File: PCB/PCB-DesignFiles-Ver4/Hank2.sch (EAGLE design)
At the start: 119 parts, among them T1 2n2222, T2 2n2222, T3 2n2222, T4 2n2222, T5 2n2222, T6 2n2222, T7 2n2222, T8 2n2222

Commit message: Mods added to pcb finished, now route the PCB
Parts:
- removed BREAKOUT: (no value), con-lstb:MA10-2
- removed C_OLED: 0.1uF, rcl:C-US025-024X044
- removed JTAG: (no value), con-lstb:MA03-2
- removed J_3V3V: Jumper, con-molex:22-23-2021
- removed LED1, LED2: (no value), led:LED3MM
- removed PR_5V1, PR_5V2, R_NI1, R_UTX1: 1k, rcl:R-US_0207/10
- removed R_NI2, R_UTX2: 2K, rcl:R-US_0207/10
- removed SSR1, SSR2, SSR3, SSR4, SSR5, SSR6, SSR7, SSR8: SSR, HankLibraries:SSR
- removed U$7: SD_CARD_READER, HankLibraries:SD_CARD_READER
- added ASC: LM358, SparkFun-IC-Amplifiers:LM358
- added C_RTC1: 0.1uF, rcl:C-US025-024X044
- added I2CR1, I2CR2: 4.7K, rcl:R-US_0207/10
- added I2C_BUS: (no value), con-lstb:MA04-1
- added LS11, LS12, LS21, LS22, LS31, LS32: 10K, rcl:R-US_0207/10
- added LSQ1, LSQ2, LSQ3: BSS138, adafruit:MOSFET-NREFLOW
- added SA1, SA2: 1k, rcl:R-US_0207/10
- added SAD1, SAD2: (no value), led:LED3MM
- added SC11: 51.5K, rcl:R-US_0207/10
- added SC12, SC22: 100k, rcl:R-US_0207/10
- added SC21: 51k1, rcl:R-US_0207/10
- added SV2, SV3: (no value), con-lstb:MA03-1
- added U$10, U$11, U$12, U$13, U$5, U$8, U$9: SSR, HankLibrariesV2:SSR
- added U$14: MA19-1, con-lstb:MA19-1
- added U$15: SD_CARD_READER, HankLibrariesV2:SD_CARD_READER
- RO12: value 150 -> 10k
- RO22, RO32, RO42, RO62, RO72, RO82: value 150 -> 10K
- U$1: value FLASH_MEMORY -> MA19-1; device HankLibraries:FLASH_MEMORY -> con-lstb:MA19-1
- U$4: value BLUETOOTH -> SSR; device HankLibraries:BLUETOOTH -> HankLibrariesV2:SSR
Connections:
- removed net FLASH_CLK: BREAKOUT.4, U$1.CLK
- removed net FLASH_CS: BREAKOUT.2, U$1.CS
- removed net FLASH_DI: BREAKOUT.6, U$1.DI
- removed net FLASH_DO: BREAKOUT.8, U$1.DO
- removed net N$1: BREAKOUT.1, J_5V-2.S
- removed net N$2: BREAKOUT.3, J_3V3V-2.S
- removed net N$39: IO_UC.(PCI2/SS/OC1B)PB2, R_NI1.2
- removed net NEW_IN: BREAKOUT.11, R_NI1.1, R_NI2.1
- removed net U_TX_3: BREAKOUT.15, R_UTX1.1, R_UTX2.2
- new net 3V3_OUT_ESP32: U$1.19, U$3.3V3
- new net 5V_BOARD: J_5V-2.S, U$1.1, U$3.5V
- new net EN_ESP32: U$1.18, U$3.EN
- new net L_AUTOMANUAL: LS31.1, LSQ3.S, U$1.9, U$3.IO27
- new net L_URX: LS11.1, LSQ1.S, U$14.9, U$3.IO17
- new net L_UTX: LS21.1, LSQ2.S, U$14.8, U$3.IO16
- new net N$38: SC21.2, SV2.3
- new net N$43: ASCG2.+IN, SC11.1, SC12.2
- new net N$44: ASCG1.+IN, SC21.1, SC22.2
- new net N$47: SC11.2, SV3.3
- new net PRESS_SEN1: ASCG2.-IN, ASCG2.OUT, U$1.17, U$3.SVP
- new net PRESS_SEN2: ASCG1.-IN, ASCG1.OUT, U$1.16, U$3.SVN
- new net SPARE_IO0: U$14.6, U$3.IO0
- new net SPARE_IO1: U$14.16, U$3.TXD0
- new net SPARE_IO10: U$1.3, U$3.SD3
- new net SPARE_IO11: U$1.2, U$3.CMD
- new net SPARE_IO12: U$1.7, U$3.IO12
- new net SPARE_IO13: U$1.5, U$3.IO13
- new net SPARE_IO14: U$1.8, U$3.IO14
- new net SPARE_IO15: U$14.4, U$3.IO15
- new net SPARE_IO2: U$14.5, U$3.IO2
- new net SPARE_IO3: U$14.15, U$3.RXD0
- new net SPARE_IO34: U$1.15, U$3.IO34
- new net SPARE_IO35: U$1.14, U$3.IO35
- new net SPARE_IO6: U$14.1, U$3.CLK
- new net SPARE_IO7: U$14.2, U$3.SD0
- new net SPARE_IO8: U$14.3, U$3.SD1
- new net SPARE_IO9: U$1.4, U$3.SD2
- new net U_SPARE: IO_UC.(PCI2/SS/OC1B)PB2
- net +3V3: now also C_RTC1.1, I2CR1.2, I2CR2.2, I2C_BUS.3, LS11.2, LS21.2, LS31.2, LSQ1.G, LSQ2.G, LSQ3.G, U$2.+3.3V; no longer C_OLED.1, C_USD.1, J_3V3V-1.S, U$1.+3.3V, U$1.HOLD, U$1.WP, U$4.+3.3V, U$7.+3.3V
- net +5V: now also ASCG3.P$V+, C_USD.1, LS12.2, LS22.2, LS32.2, SV2.2, SV3.2, U$10.+, U$11.+, U$12.+, U$13.+, U$15.+5V, U$4.+, U$5.+, U$8.+, U$9.+; no longer JTAG.2, SSR1.+, SSR2.+, SSR3.+, SSR4.+, SSR5.+, SSR6.+, SSR7.+, SSR8.+
- net AUTO_MANUAL: now also LS32.1, LSQ3.D; no longer BREAKOUT.20, JTAG.4
- net BT_RX: now also U$14.7, U$2.RXD, U$3.IO4; no longer BREAKOUT.7, U$4.RXD
- net BT_TX: now also U$1.11, U$2.TXD, U$3.IO25; no longer BREAKOUT.9, U$4.TXD
- net GND: now also ASCG3.P$V-, C_RTC1.2, I2C_BUS.4, SA1.1, SA2.1, SC12.1, SC22.1, SV2.1, SV3.1, U$1.6, U$14.13, U$14.19, U$15.GND, U$2.GND, U$3.GND@14, U$3.GND@32, U$3.GND@38; no longer BREAKOUT.5, C_OLED.2, JTAG.6, PR_5V1.1, PR_5V2.1, R_NI2.2, R_UTX2.1, U$1.GND, U$4.GND, U$7.GND
- net IN7: no longer JTAG.1
- net IN8: no longer JTAG.3
- net L1-1: now also U$10.L1, U$4.L1, U$5.L1, U$8.L1; no longer SSR1.L1, SSR2.L1, SSR3.L1, SSR4.L1
- net L1-2: now also U$11.L1, U$12.L1, U$13.L1, U$9.L1; no longer SSR5.L1, SSR6.L1, SSR7.L1, SSR8.L1
- net LED2: now also SA2.2, SAD2.C; no longer LED2.C, PR_5V2.2
- net L_O1: now also U$8.-; no longer SSR2.-
- net L_O3: now also U$5.-; no longer SSR3.-
- net MISO: now also U$14.12, U$15.MISO, U$3.IO19; no longer BREAKOUT.10, U$7.MISO
- net MOSI: now also U$14.18, U$15.MOSI, U$3.IO23; no longer BREAKOUT.12, U$7.MOSI
- net N$10: now also U$13.L2; no longer SSR8.L2
- net N$12: now also U$9.-; no longer SSR5.-
- net N$13: now also U$12.L2; no longer SSR7.L2
- net N$14: now also U$8.L2; no longer SSR2.L2
- net N$15: now also U$5.L2; no longer SSR3.L2
- net N$17: now also U$11.-; no longer SSR6.-
- net N$19: now also U$11.L2; no longer SSR6.L2
- net N$21: now also U$12.-; no longer SSR7.-
- net N$24: now also U$10.L2; no longer SSR4.L2
- net N$26: now also U$13.-; no longer SSR8.-
- net N$28: now also U$9.L2; no longer SSR5.L2
- net N$3: now also U$4.L2; no longer SSR1.L2
- net N$30: now also U$4.-; no longer SSR1.-
- net N$42: now also U$10.-; no longer SSR4.-
- net N$6: now also SA1.2, SAD1.C; no longer LED1.C, PR_5V1.2
- net SCK: now also U$14.11, U$15.SCK, U$3.IO18; no longer BREAKOUT.14, U$7.SCK
- net SCL: now also I2CR1.1, I2C_BUS.1, U$14.17, U$3.IO22; no longer BREAKOUT.19
- net SDA: now also I2CR2.1, I2C_BUS.2, U$14.14, U$3.IO21; no longer BREAKOUT.17
- net SD_CS: now also U$14.10, U$15.CS, U$3.IO5; no longer BREAKOUT.16, U$7.CS
- net STAY_ALIVE1: now also SAD1.A, U$1.13, U$3.IO32; no longer LED1.A
- net STAY_ALIVE2: now also SAD2.A, U$1.12, U$3.IO33; no longer LED2.A
- net TEMP_SEN: now also U$1.10, U$3.IO26; no longer BREAKOUT.18
- net U_RESET: no longer JTAG.5
- net U_RX: now also LS12.1, LSQ1.D; no longer BREAKOUT.13
- net U_TX: now also LS22.1, LSQ2.D; no longer R_UTX1.2
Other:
- note added: "11/02/2021"
- note added: "4.0"
- note added: "ADC Signal Conditioning"
- note added: "Aux IO Control - Arduino based"
- note added: "Bluetooth Serial Port"
- note added: "Change Log: 1. Removed JLCJLC that was used by manufacturer 2. Changed Positions of the labels on PCB to readable 3. Changed the bluetooth pins 4. TODO Replaced Transistor in SSR outputs 5. Changed Resistance in the base of transistor for 10K 6. Jumpers renamed 7. SSR footprint was adjusted 8. Added level converters between ESP32 and ATMega 9. Added 2 LEDs for stay alive signals 10. TODO Renamed 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"
- note added: "ESP32 Dev Kit"
- note added: "I2C Bus Display - RTC - Spare I2C Bus"
- note added: "JVivas01.20210211"
- note added: "Level Shifters"
- note added: "Low Level Toward ESP32"
- note added: "Low Level Towards ATMega"
- note added: "Micro SD Card"
- note added: "Powe supplies"
- note added: "Solid State Relays"
- note added: "Temperature Sensor"
- note added: "User Inputs and Indicators"
- note removed: "/RESET"
- note removed: "MISO"
- note removed: "MOSI"
- note removed: "Released under the Creative Commons Attribution Share-Alike 3.0 License"
- note removed: "SCK"
- moved on the sheet: AUTO-1, AUTO-2, CP01, CP31, CP51, C_BT, C_FM, C_RTC, C_U, C_URTS, C_USD, C_UXTAL1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

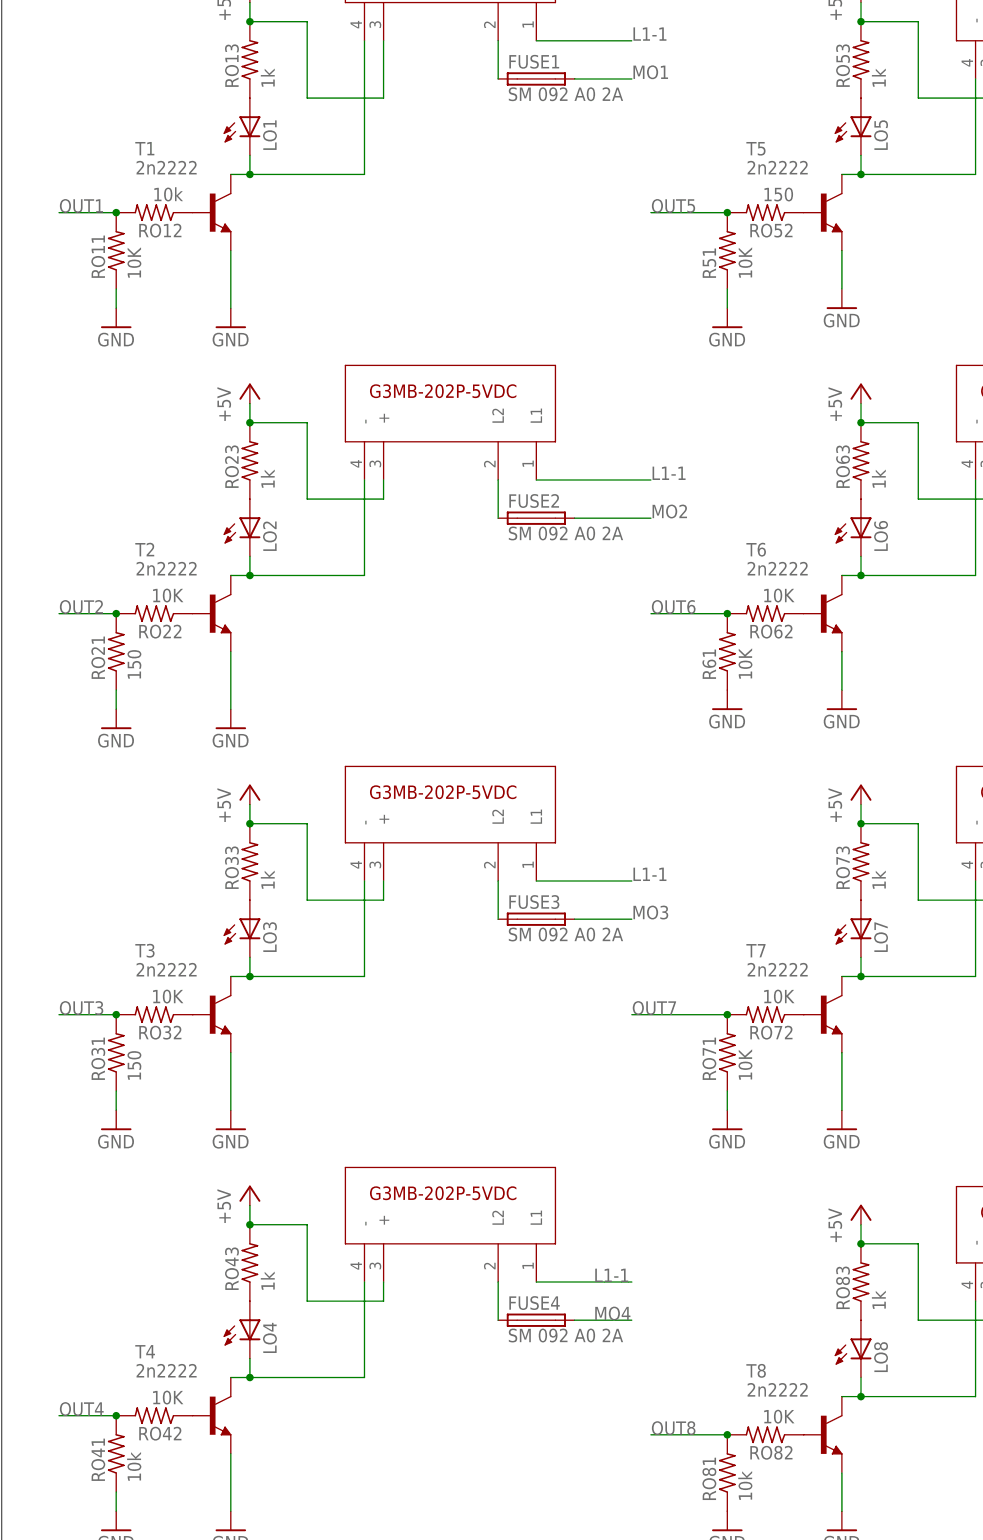
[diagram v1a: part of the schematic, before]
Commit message: Changes to the transistorss footprint, ready to route
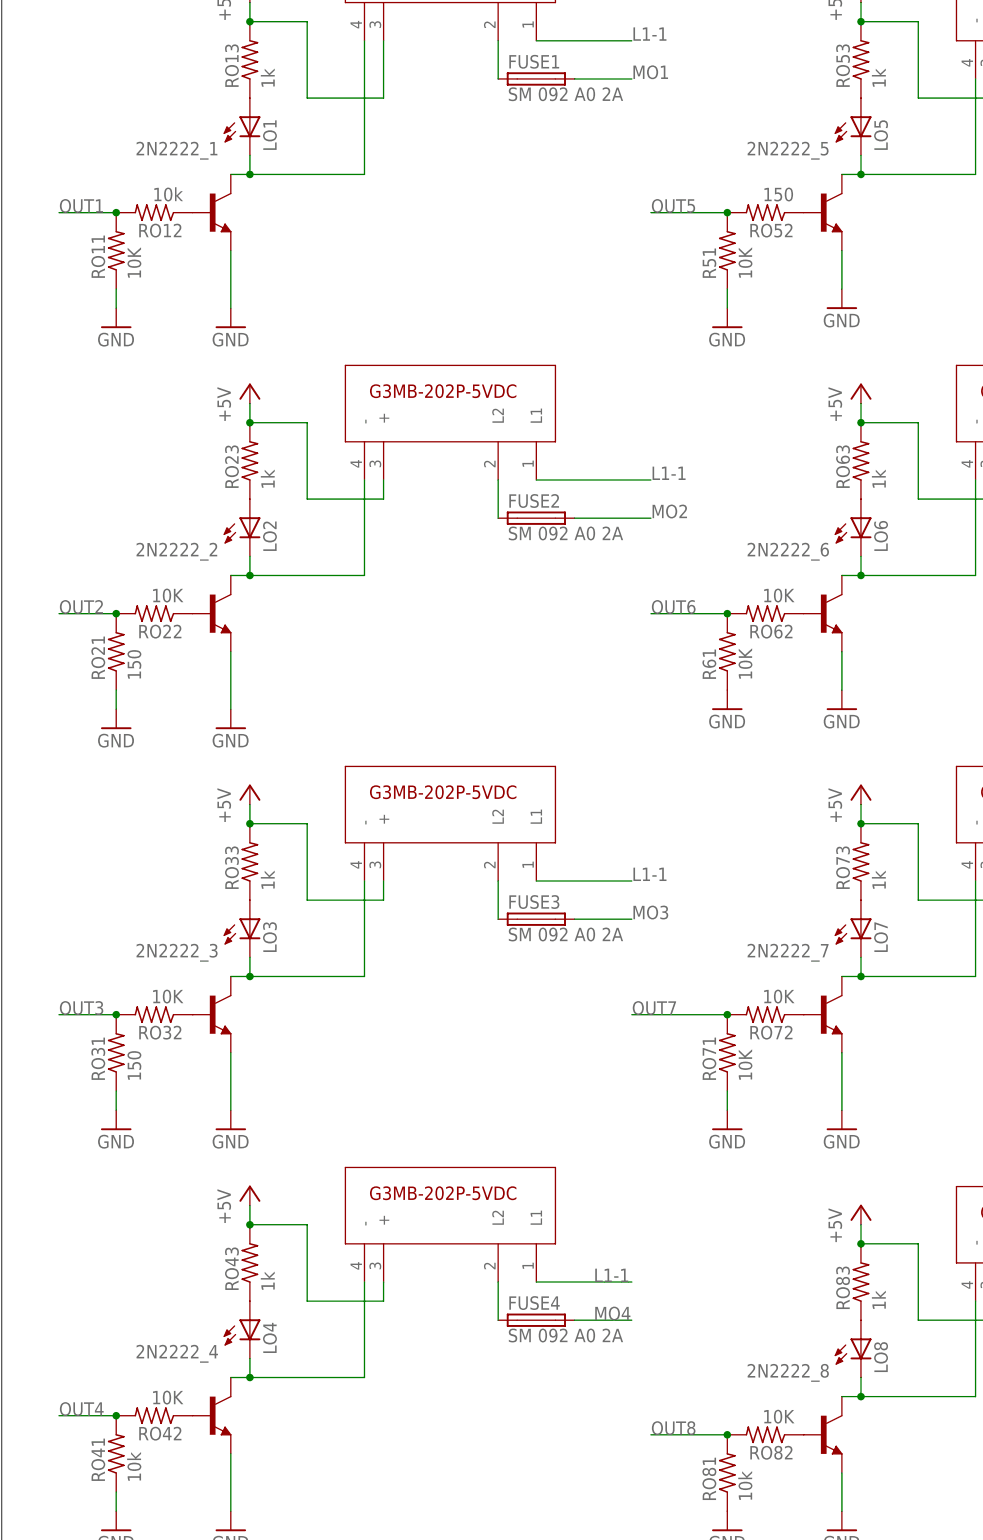
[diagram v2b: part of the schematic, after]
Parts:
- removed T1, T2, T3, T4, T5, T6, T7, T8: 2n2222, transistor:2SC458
- added 2N2222_1, 2N2222_2, 2N2222_3, 2N2222_4, 2N2222_5, 2N2222_6, 2N2222_7, 2N2222_8: (no value), transistor:-NPN-TO92-EBC
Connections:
- removed net N$17: LO6.C, T6.C, U$11.-
- removed net N$34: RO82.1, T8.B
- new net 2N2222_6: 2N2222_6.C, LO6.C, U$11.-
- new net N$2: 2N2222_1.B, RO12.1
- net GND: now also 2N2222_1.E, 2N2222_2.E, 2N2222_3.E, 2N2222_4.E, 2N2222_5.E, 2N2222_6.E, 2N2222_7.E, 2N2222_8.E; no longer T1.E, T2.E, T3.E, T4.E, T5.E, T6.E, T7.E, T8.E
- net L_O1: now also 2N2222_2.C; no longer T2.C
- net L_O3: now also 2N2222_3.C; no longer T3.C
- net N$12: now also 2N2222_5.C; no longer T5.C
- net N$18: now also 2N2222_2.B, RO22.1; no longer RO62.1, T6.B
- net N$21: now also 2N2222_7.C; no longer T7.C
- net N$22: now also 2N2222_7.B; no longer T7.B
- net N$23: now also 2N2222_3.B, RO32.1; no longer RO42.1, T4.B
- net N$26: now also 2N2222_8.C; no longer T8.C
- net N$27: now also 2N2222_4.B, RO42.1; no longer RO32.1, T3.B
- net N$30: now also 2N2222_1.C; no longer T1.C
- net N$31: now also 2N2222_8.B, RO82.1; no longer RO22.1, T2.B
- net N$42: now also 2N2222_4.C; no longer T4.C
- net N$8: now also 2N2222_5.B, RO52.1; no longer RO12.1, T1.B
- net N$9: now also 2N2222_6.B, RO62.1; no longer RO52.1, T5.B
